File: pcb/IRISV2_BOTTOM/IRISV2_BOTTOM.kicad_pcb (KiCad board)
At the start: 4 copper layers, 50 x 50 mm, 71 parts, among them J1 Screw_Terminal_01x02, Q1 BC846, Q10 PJA3404A, Q11 PJA3404A, Q12 PJA3404A, Q13 BC846, Q14 MCAC011P03L-TP, Q15 BC846, Q16 MCAC011P03L-TP, Q2 BC846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

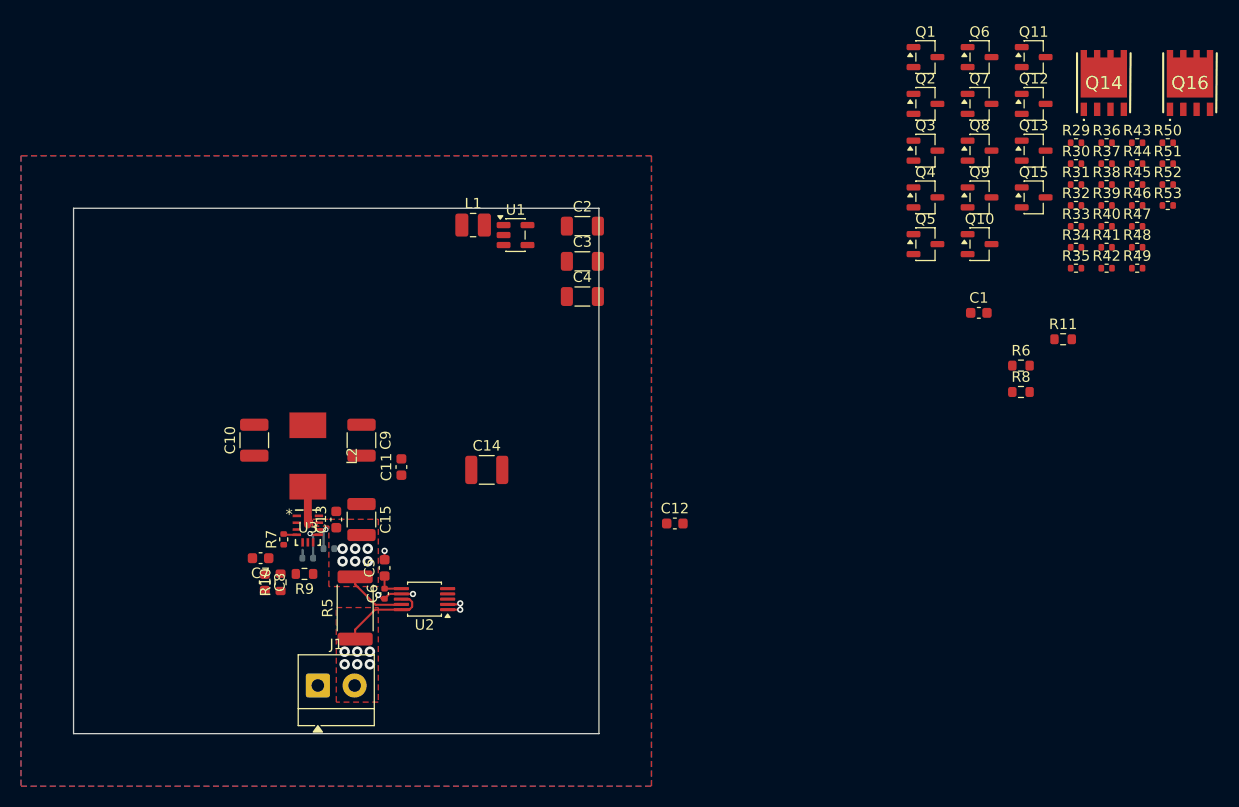
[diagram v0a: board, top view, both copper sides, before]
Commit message: bottom pcb now mostly done, connectors selected - now need to finish integrating the connectors and other small tweaks to bottom routing
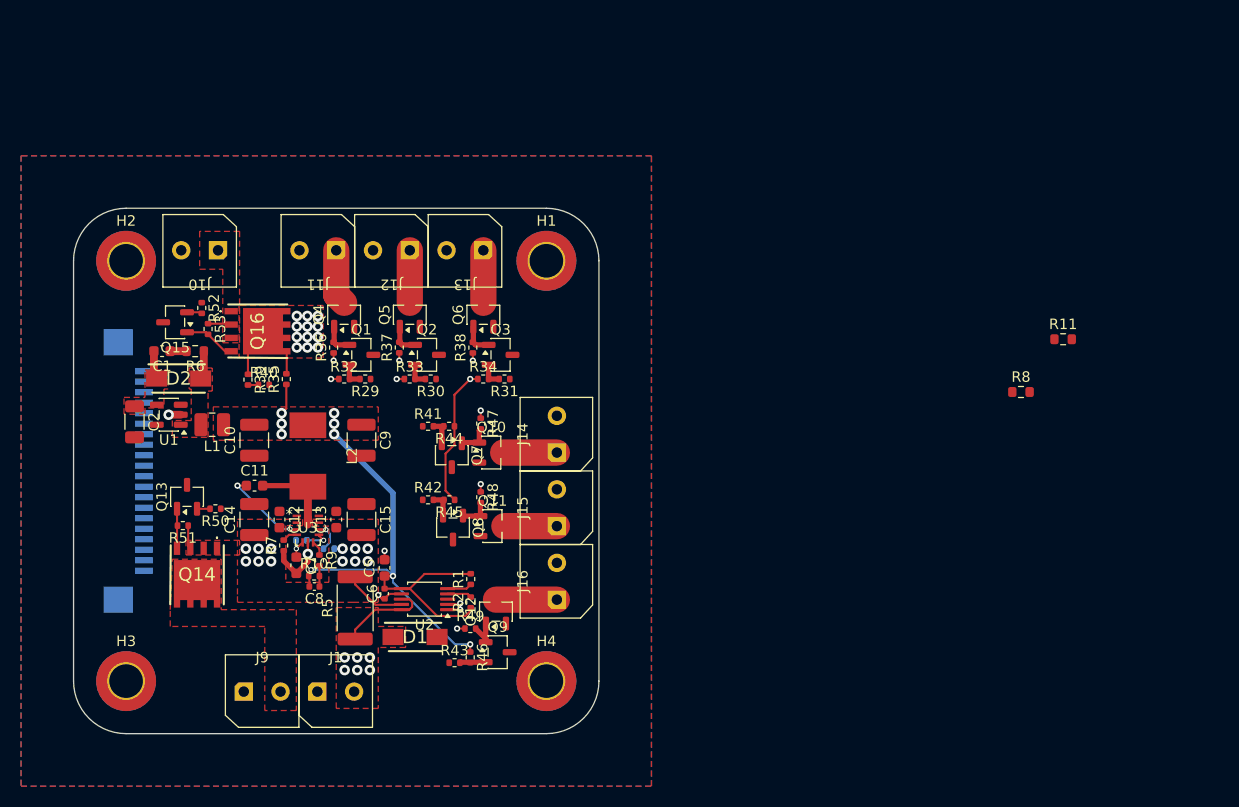
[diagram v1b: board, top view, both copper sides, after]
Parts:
- removed C3, C4: 10uF, Capacitor_SMD:C_1206_3216Metric
- added D1: D_Schottky, SK34SMA-3G:DIOM5027X240N, F.Cu at (162.5, 120.8)
- added D2: D_Schottky, SK34SMA-3G:DIOM5027X240N, F.Cu at (140.0, 96.2)
- added H1: MountingHole_Pad, MountingHole:MountingHole_3.2mm_M3_ISO7380_Pad_TopBottom, F.Cu at (175.0, 85.0)
- added H2: MountingHole_Pad, MountingHole:MountingHole_3.2mm_M3_ISO7380_Pad_TopBottom, F.Cu at (135.0, 85.0)
- added H3: MountingHole_Pad, MountingHole:MountingHole_3.2mm_M3_ISO7380_Pad_TopBottom, F.Cu at (135.0, 125.0)
- added H4: MountingHole_Pad, MountingHole:MountingHole_3.2mm_M3_ISO7380_Pad_TopBottom, F.Cu at (175.0, 125.0)
- added J10: Screw_Terminal_01x02, kf350-2p:kf350-2p, F.Cu at (142.0, 84.0)
- added J11: Screw_Terminal_01x02, kf350-2p:kf350-2p, F.Cu at (153.2, 84.0)
- added J12: Screw_Terminal_01x02, kf350-2p:kf350-2p, F.Cu at (160.2, 84.0)
- added J13: Screw_Terminal_01x02, kf350-2p:kf350-2p, F.Cu at (167.2, 84.0)
- added J14: Screw_Terminal_01x02, kf350-2p:kf350-2p, F.Cu at (176.0, 101.5)
- added J15: Screw_Terminal_01x02, kf350-2p:kf350-2p, F.Cu at (176.0, 108.5)
- added J16: Screw_Terminal_01x02, kf350-2p:kf350-2p, F.Cu at (176.0, 115.5)
- added J3: Conn_01x20_MountingPin, FFC3B07-20-T:FFC3B07-20-T, B.Cu at (136.7, 105.0)
- added J9: Screw_Terminal_01x02, kf350-2p:kf350-2p, F.Cu at (147.9, 126.0)
- added R1: 4.7k, Resistor_SMD:R_0402_1005Metric, F.Cu at (167.8, 115.3)
- added R2: 4.7k, Resistor_SMD:R_0402_1005Metric, F.Cu at (167.8, 117.5)
- C2: value 10uF -> 22uF
- C8: footprint Capacitor_SMD:C_0603_1608Metric -> Capacitor_SMD:C_0402_1005Metric
- J1: footprint TerminalBlock_MetzConnect:TerminalBlock_MetzConnect_Type059_RT06302HBWC_1x02_P3.50mm_Horizontal -> kf350-2p:kf350-2p
- R10, R9: footprint Resistor_SMD:R_0603_1608Metric -> Resistor_SMD:R_0402_1005Metric
- moved R51 99.9 mm to (140.4, 110.2), turned to 180 degrees
- moved Q14 98.3 mm to (141.8, 115.0), turned to 180 degrees
- moved R50 97.1 mm to (143.5, 108.6), turned to 180 degrees
- moved R52 92.7 mm to (142.2, 89.5), turned to -90 degrees
- moved R53 92.1 mm to (142.8, 91.5), turned to -90 degrees
- moved Q16 91.7 mm to (147.6, 91.7), turned to -90 degrees
- moved Q13 87.1 mm to (140.8, 107.5), turned to 90 degrees
- moved R39 83.4 mm to (146.6, 96.3), turned to -90 degrees
- moved Q15 82.6 mm to (139.7, 90.8), turned to 180 degrees
- moved R43 81.7 mm to (166.3, 123.2)
- moved R40 81.6 mm to (148.1, 96.8)
- moved R6 78.6 mm to (141.6, 93.6), turned to 180 degrees
- moved C1 77.8 mm to (138.4, 93.6), turned to 180 degrees
- moved R46 76.7 mm to (167.8, 122.7), turned to -90 degrees
- moved R36 76.1 mm to (154.8, 93.3), turned to 90 degrees
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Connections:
- net Net-(D2-A) renamed /switch
- net Net-(J10-Pin_1) renamed /power_control/controlled_batt
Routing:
- net +3.3V: track 2.80 -> 72.8 mm, vias 0 -> 12
- net /bootstrap: track 0.00 -> 8.23 mm, vias 0 -> 2
- net /power_control/cx_high: track 0.00 -> 6.84 mm, vias 0 -> 12
- net GND: track 6.94 -> 13.0 mm, vias 5 -> 6
- net /power_control/c6_-: track 0.00 -> 5.80 mm
- net /power_control/c1_-: track 0.00 -> 5.31 mm
- net /power_control/c4_-: track 0.00 -> 5.11 mm
- net /power_control/c5_-: track 0.00 -> 5.00 mm
- net /power_control/c3_-: track 0.00 -> 5.00 mm
- net /power_control/c2_-: track 0.00 -> 5.00 mm
- net Net-(Q15-C): track 0.00 -> 4.95 mm
- net +BATT: track 8.82 -> 13.2 mm, vias 6 -> 12
- net Net-(U3-SW): track 3.60 -> 7.94 mm
- net Net-(Q13-C): track 0.00 -> 3.76 mm
- net Net-(Q12-G): track 0.00 -> 3.48 mm
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- added copper zone on F.Cu, net +3.3V
- added copper zone on In1.Cu, net +3.3V
- added copper zone on F.Cu, net +5V
- added copper zone on F.Cu, net /power_control/cam_pow
- added copper zone on F.Cu, net /power_control/controlled_batt
- added copper zone on F.Cu, net /power_control/cx_high
- added copper zone on F.Cu, net /switch
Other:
- outline, holes or cut-outs redrawn

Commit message: bottom board design done, need to polish it
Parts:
- added BZ1: Buzzer, CMT-8504-03-SMT:CMT850403SMTTR, B.Cu at (155.0, 105.0)
- added D3: 3.3_GOOD, LED_SMD:LED_0805_2012Metric, F.Cu at (174.5, 96.2)
- added D4: 5_GOOD, LED_SMD:LED_0805_2012Metric, F.Cu at (174.5, 92.5)
- added Q17: BC846, Package_TO_SOT_SMD:SOT-23-3, B.Cu at (162.8, 103.8)
- added R3: 1k, Resistor_SMD:R_0402_1005Metric, B.Cu at (165.0, 103.0)
- added R4: 10k, Resistor_SMD:R_0402_1005Metric, B.Cu at (166.5, 102.5)
- moved R11 46.3 mm to (177.9, 92.5), turned to 180 degrees
- moved R8 42.4 mm to (177.8, 96.2), turned to 180 degrees
- moved R7 0.25 mm to (149.8, 112.1)
- moved C7 0.20 mm to (151.0, 114.0)
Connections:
- J3 pad 20: GND -> buzzer
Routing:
- net +5VP: track 0.00 -> 51.6 mm, vias 0 -> 4
- net +5V: track 2.70 -> 54.2 mm, vias 0 -> 3
- net c6_fire: track 0.00 -> 50.8 mm, vias 0 -> 1
- net c4_fire: track 0.00 -> 48.1 mm, vias 0 -> 1
- net c3_fire: track 0.00 -> 41.8 mm, vias 0 -> 1
- net ina_sda: track 2.32 -> 40.4 mm, vias 0 -> 1
- net c2_fire: track 0.00 -> 35.3 mm, vias 0 -> 1
- net ina_scl: track 2.37 -> 35.6 mm, vias 0 -> 1
- net buzzer: track 0.00 -> 32.1 mm, vias 0 -> 2
- net c5_fire: track 0.00 -> 31.7 mm, vias 0 -> 2
- net c1_fire: track 0.00 -> 28.9 mm, vias 0 -> 1
- net +3.3V: track 72.8 -> 95.5 mm
- net arm: track 0.00 -> 21.7 mm, vias 0 -> 1
- net /power_control/cx_high: track 6.84 -> 26.7 mm
- net cont_test: track 1.01 -> 12.8 mm, vias 0 -> 2
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- added copper zone on In2.Cu, net /power_control/cx_high

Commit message: bottom board pending sanity check but done
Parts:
- renumbered H2 to 3v3, H1 to 3v3, H3 to GND, H4 to GND
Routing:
- net GND: track 19.7 -> 20.3 mm
